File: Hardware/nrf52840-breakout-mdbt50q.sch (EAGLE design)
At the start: 49 parts, among them J8 CORTEX_DEBUG_PTH, U1 MDBT50Q, U2 MCP73831, U3 3.3V, Y1 32.768kHz

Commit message: Revisions preparing for v10
- Rearranged pin breakouts, qwiic connection, LED, and button
- Flipped on/off switch towards module for easier access
- Expanded board 50mil to facilitate soldering pins near buttons
- Labeled pins on top side
- Increased VBAT and VUSB power trace width
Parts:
- added J12: (no value), SparkFun-Connectors:CONN_021X02_NO_SILK
- LOGO1: value SPARKX-LOGO3 -> SFE_LOGO_NAME.2_INCH; device SparkX:SPARKX-LOGO3 -> SparkFun-Aesthetics:SFE_LOGO_NAME.2_INCH
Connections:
- net N$2 renamed VREG_EN
- new net P0.07: R3.2, U1.P0.07(TRACECLK)
- net GND: now also J12.1, S2.O; no longer S2.S
- net P0.06: no longer R3.2
- net P0.08: now also J3.3; no longer J5.2
- net P0.11: now also J3.4; no longer J5.1
- net P0.13: now also R7.1, S3.2; no longer J7.7
- net P0.15: now also J5.1; no longer J7.6
- net P0.17: now also J5.2; no longer J7.5
- net P0.19: now also J7.7; no longer J7.4
- net P0.20: now also J7.6; no longer J3.3
- net P0.21: now also J7.5; no longer J7.3
- net P0.22: now also J7.4; no longer R7.1, S3.2
- net P0.23: now also J7.3; no longer J3.4
- net P0.29/AIN5: now also J2.5; no longer J2.3
- net P0.30/AIN6: now also J2.4; no longer J2.5
- net P0.31/AIN7: now also J2.3; no longer J2.4
- net VIN: now also S2.S; no longer S2.O
- net V_BATT: now also J12.2
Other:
- note added: "3.3V Regulator"
- note added: "Buttons"
- note added: "Headers"
- note added: "I2C/Qwiic"
- note added: "NFC Capacitors (DNP)"
- note added: "Power Source Select"
- note added: "SWD Program/Debug Interface"
- note added: "USB/LiPo Charger"
- note added: "Unpopulated NFC caps: External caps to tune antenna resonance to 13.56MHz. Recommended: 130pF"
- note added: "User LED"
- note added: "nRF52840 (MDBT50Q)"
- note added: "v10"
- note removed: "x01"
- moved on the sheet: C1, C2, C4, D3, D4, J1, J10, J11, J2, J3, J4, J5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

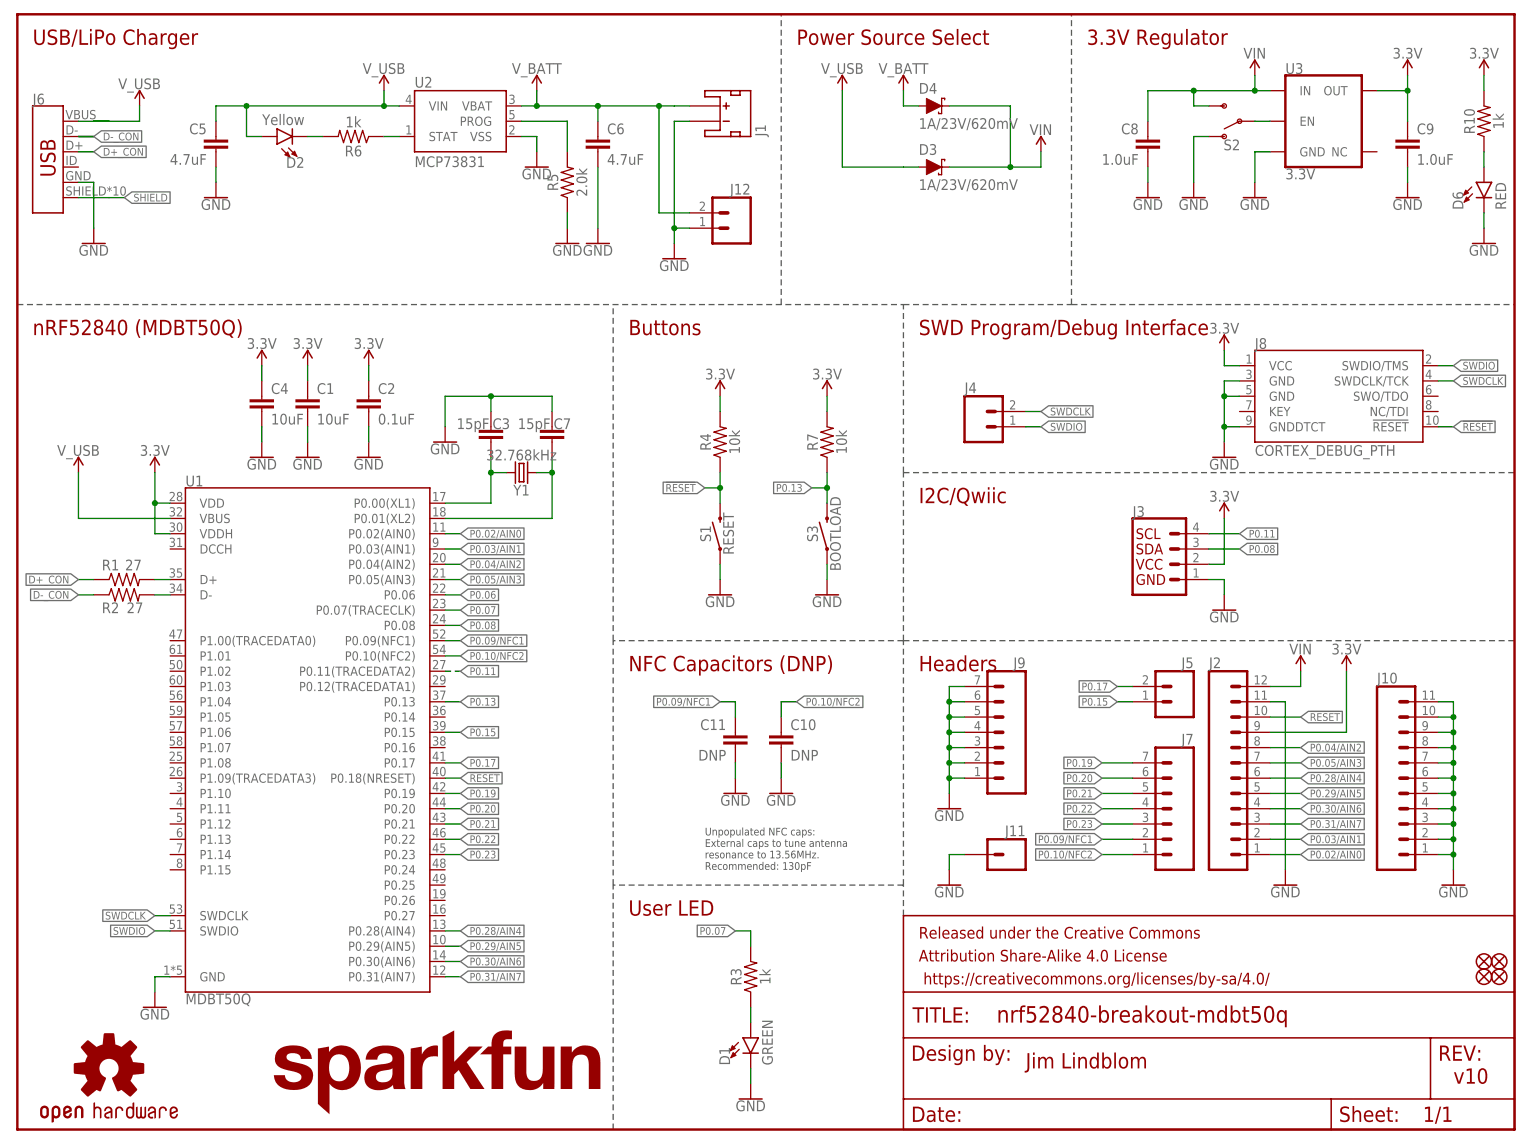
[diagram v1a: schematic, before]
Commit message: Board revisions post engineer checklist
- Added extra ground PTH
- Added production sku for nRF module
- Added link to tutorial
- Clean up schematic
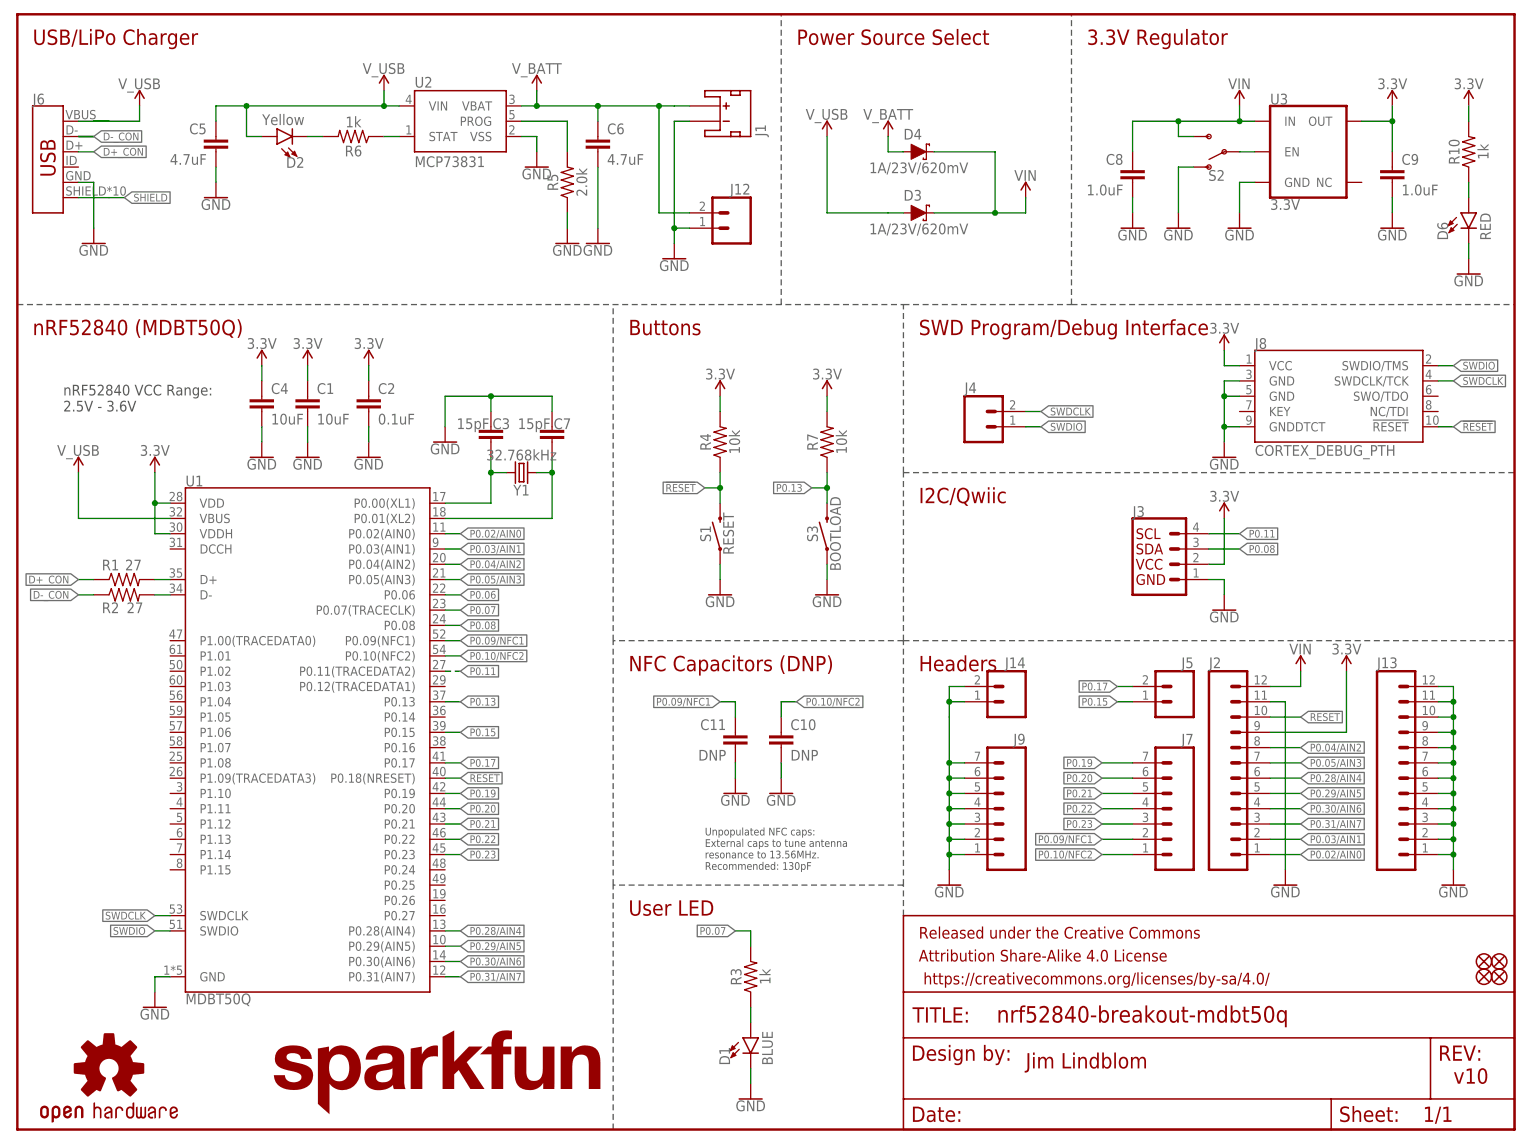
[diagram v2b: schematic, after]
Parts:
- removed J10: (no value), SparkFun-Connectors:CONN_111X11_NO_SILK
- removed J11: (no value), SparkFun-Connectors:CONN_01PTH_NO_SILK_YES_STOP
- added J13: (no value), SparkFun-Connectors:CONN_12NO_SILK
- added J14: (no value), SparkFun-Connectors:CONN_021X02_NO_SILK
- D1: value GREEN -> BLUE; device SparkFun-LED:LED-GREEN0603 -> SparkFun-LED:LED-BLUE0603
- LOGO2: value OSHW-LOGOM -> OSHW-LOGOS; device SparkFun-Aesthetics:OSHW-LOGOM -> SparkFun-Aesthetics:OSHW-LOGOS
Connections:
- net GND: now also J13.1, J13.10, J13.11, J13.12, J13.2, J13.3, J13.4, J13.5, J13.6, J13.7, J13.8, J13.9, J14.1, J14.2; no longer J10.1, J10.10, J10.11, J10.2, J10.3, J10.4, J10.5, J10.6, J10.7, J10.8, J10.9, J11.1
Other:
- note added: "nRF52840 VCC Range: 2.5V - 3.6V"
- moved on the sheet: C8, C9, D3, D4, D6, J9, R10, S2, U3

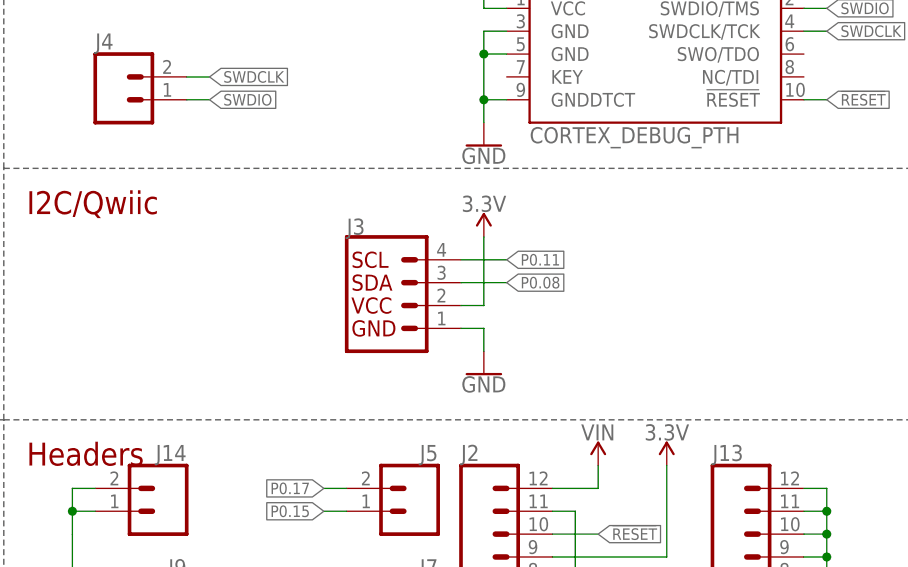
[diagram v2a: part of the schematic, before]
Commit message: Adding pull-up resistors to I2C lines.
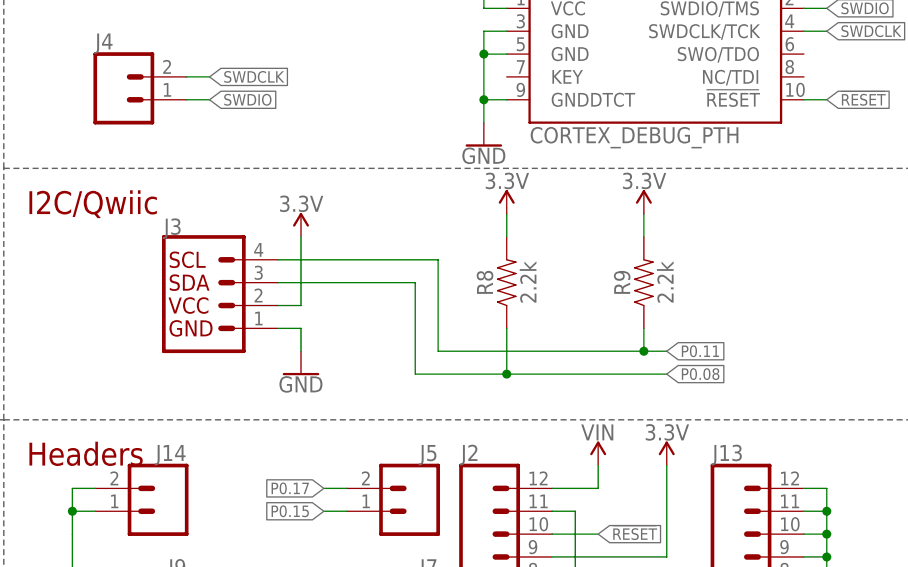
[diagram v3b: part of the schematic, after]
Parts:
- added R8, R9: 2.2k, SparkFun-Resistors:2.2KOHM-0603-1/10W-1%
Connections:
- net 3.3V: now also R8.2, R9.2
- net P0.08: now also R8.1
- net P0.11: now also R9.1
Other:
- moved on the sheet: J3
